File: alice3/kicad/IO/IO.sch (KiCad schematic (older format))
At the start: 1 part, among them U1 MiniM4-D40

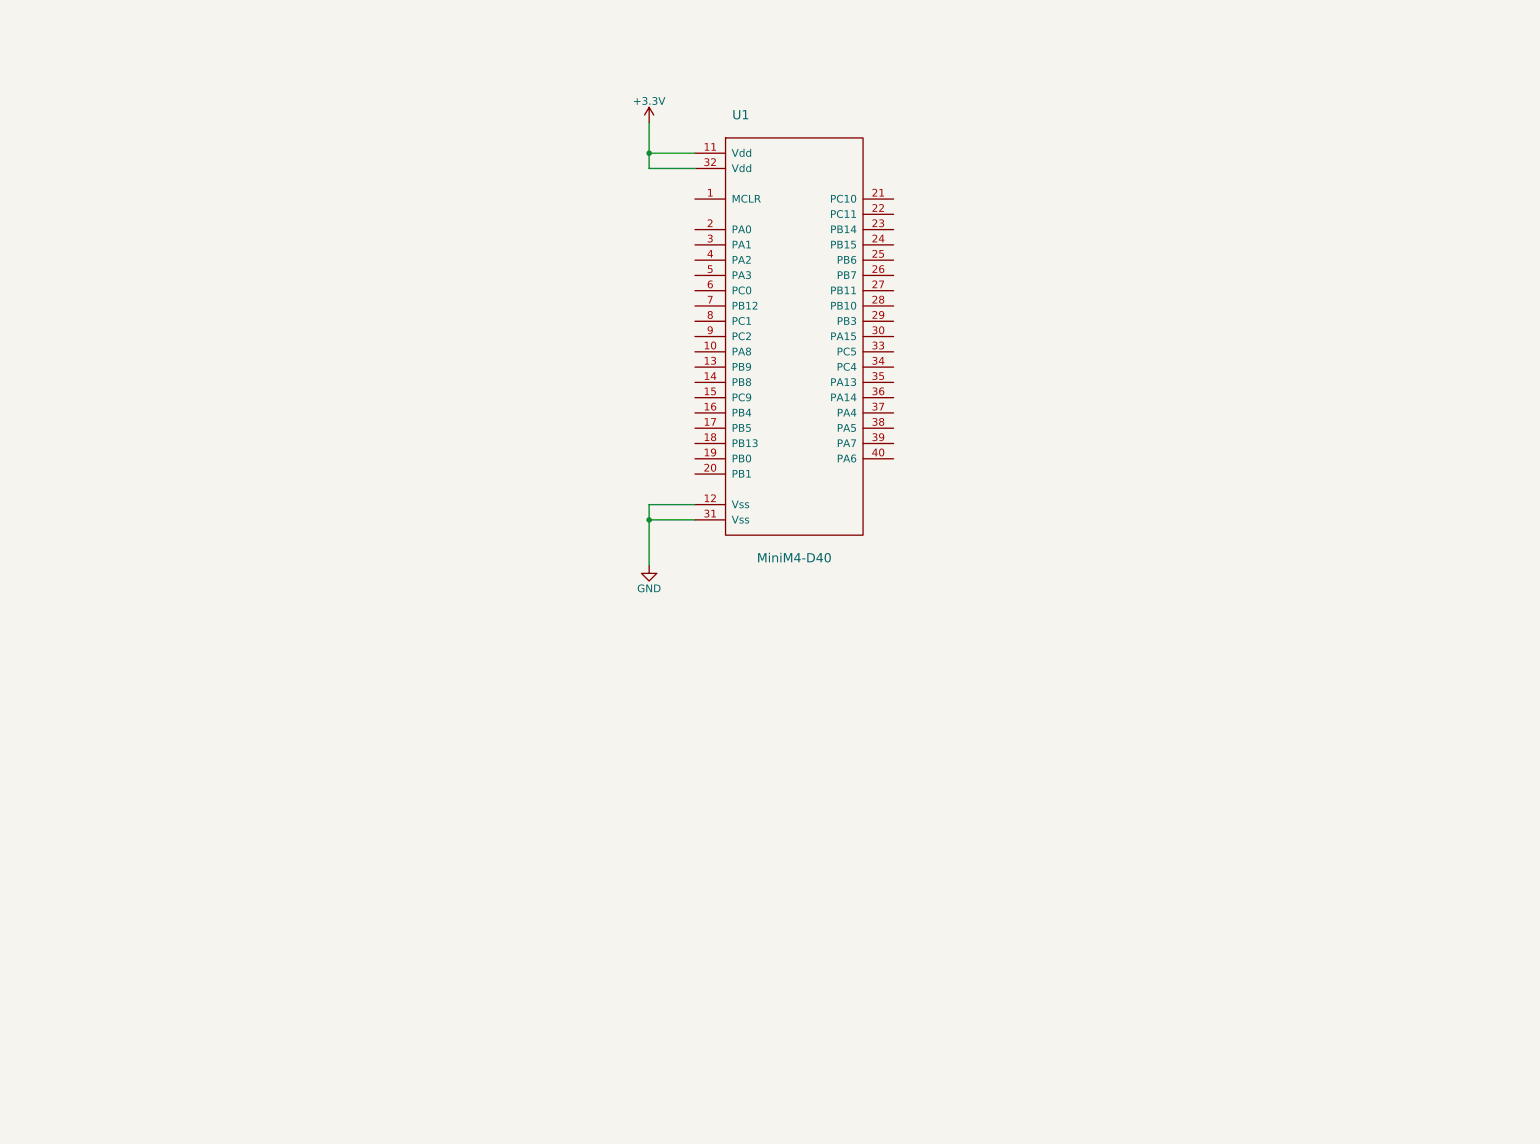
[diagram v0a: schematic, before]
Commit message: add SD socket to sch; level converter component
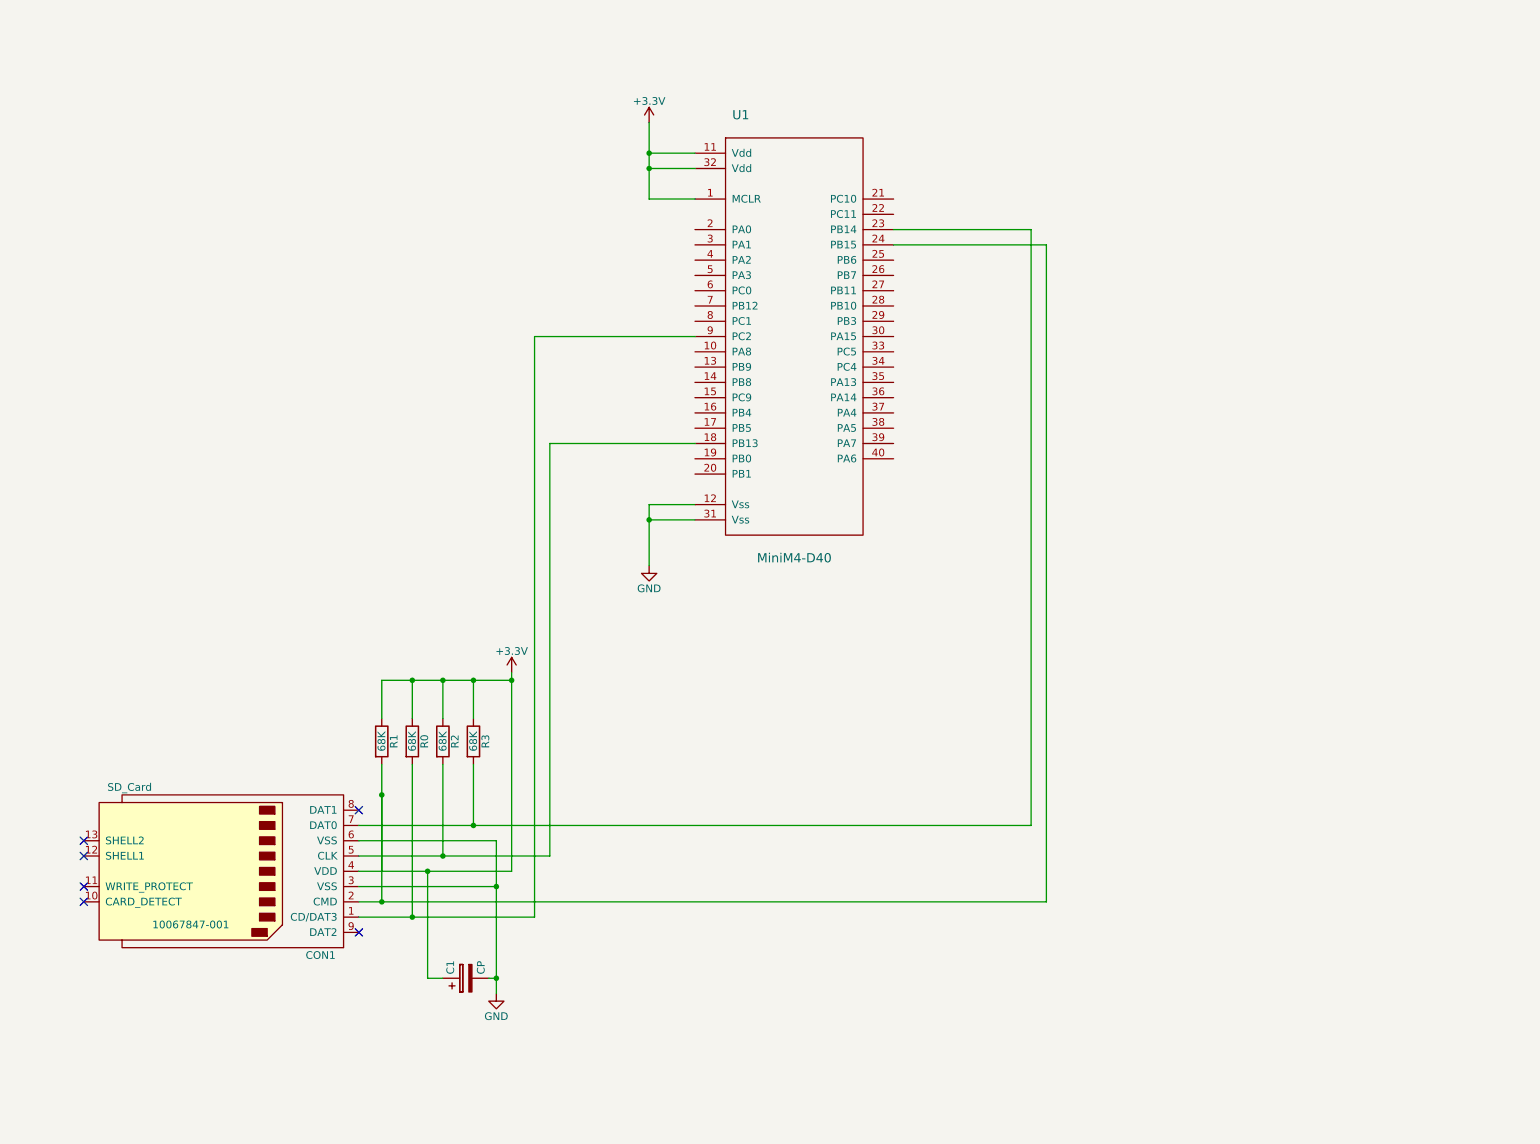
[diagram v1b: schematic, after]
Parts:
- added C1: CP, symbol CP
- added CON1: SD_Card, 10067847-001, symbol SD_Card
- added R0, R1, R2, R3: 68K, symbol R
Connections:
- net +3V3: now also U1.1 (MCLR), C1.1, CON1.4 (VDD), R0.1, R1.1, R2.1, R3.1
- net GND: now also C1.2, CON1.3 (VSS), CON1.6 (VSS)
- net at U1.18 (PB13): now also CON1.5 (CLK), R2.2
- net at U1.23 (PB14): now also CON1.7 (DAT0), R3.2
- net at U1.24 (PB15): now also CON1.2 (CMD), R1.2
- net at U1.9 (PC2): now also CON1.1 (CD/DAT3), R0.2
- no-connect marks 0 -> 6
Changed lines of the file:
@@
 LIBS:valves
 LIBS:minim4-d40
+LIBS:levelconverter
 LIBS:IO-cache
 EELAYER 25 0
@@
 $EndComp
 $Comp
-L +3.3V #PWR01
+L +3.3V #PWR3
 U 1 1 5689970E
 P 4800 1300
-F 0 "#PWR01" H 4800 1150 50  0001 C CNN
+F 0 "#PWR3" H 4800 1150 50  0001 C CNN
 F 1 "+3.3V" H 4800 1440 50  0000 C CNN
 F 2 "" H 4800 1300 60  0000 C CNN
@@
 	1    0    0    -1
 $EndComp
-Wire Wire Line
-	5100 1500 4800 1500
-Wire Wire Line
-	4800 1300 4800 1600
-Wire Wire Line
-	4800 1600 5100 1600
-Connection ~ 4800 1500
-$Comp
-L GND #PWR02
+$Comp
+L GND #PWR4
 U 1 1 5689975D
 P 4800 4200
-F 0 "#PWR02" H 4800 3950 50  0001 C CNN
+F 0 "#PWR4" H 4800 3950 50  0001 C CNN
 F 1 "GND" H 4800 4050 50  0000 C CNN
 F 2 "" H 4800 4200 60  0000 C CNN
@@
 	1    0    0    -1
 $EndComp
+$Comp
+L SD_Card CON1
+U 1 1 56899BB6
+P 2000 6200
+F 0 "CON1" H 1350 6750 50  0000 C CNN
+F 1 "SD_Card" H 2600 5650 50  0000 C CNN
+F 2 "10067847-001" H 2200 6550 50  0000 C CNN
+F 3 "" H 2000 6200 60  0000 C CNN
+	1    2000 6200
+	-1   0    0    1
+$EndComp
+NoConn ~ 1100 6000
+NoConn ~ 1100 6100
+NoConn ~ 1100 6300
+NoConn ~ 1100 6400
+NoConn ~ 2900 6600
+NoConn ~ 2900 5800
+$Comp
+L GND #PWR1
+U 1 1 56899C9B
+P 3800 7000
+F 0 "#PWR1" H 3800 6750 50  0001 C CNN
+F 1 "GND" H 3800 6850 50  0000 C CNN
+F 2 "" H 3800 7000 60  0000 C CNN
+F 3 "" H 3800 7000 60  0000 C CNN
+	1    3800 7000
+	1    0    0    -1
+$EndComp
+$Comp
+L +3.3V #PWR2
+U 1 1 56899CD4
+P 3900 4900
+F 0 "#PWR2" H 3900 4750 50  0001 C CNN
+F 1 "+3.3V" H 3900 5040 50  0000 C CNN
+F 2 "" H 3900 4900 60  0000 C CNN
+F 3 "" H 3900 4900 60  0000 C CNN
+	1    3900 4900
+	1    0    0    -1
+$EndComp
+Connection ~ 3800 6300
+Wire Wire Line
+	2900 6300 3800 6300
+Wire Wire Line
+	3800 6000 3800 7000
+Wire Wire Line
+	2900 6000 3800 6000
+Connection ~ 4800 1600
+Wire Wire Line
+	4800 1800 5100 1800
+Connection ~ 4800 3900
+Wire Wire Line
+	5100 3900 4800 3900
+Wire Wire Line
+	4800 3800 4800 4200
 Wire Wire Line
 	5100 3800 4800 3800
-Wire Wire Line
-	4800 3800 4800 4200
-Wire Wire Line
-	5100 3900 4800 3900
-Connection ~ 4800 3900
+Connection ~ 4800 1500
+Wire Wire Line
+	4800 1600 5100 1600
+Wire Wire Line
+	4800 1300 4800 1800
+Wire Wire Line
+	5100 1500 4800 1500
+Wire Wire Line
+	5100 2700 4050 2700
+Wire Wire Line
+	4050 2700 4050 6500
+Wire Wire Line
+	4050 6500 2900 6500
+Wire Wire Line
+	2900 6400 7400 6400
+Wire Wire Line
+	7400 6400 7400 2100
+Wire Wire Line
+	7400 2100 6400 2100
+Wire Wire Line
+	5100 3400 4150 3400
+Wire Wire Line
+	4150 3400 4150 6100
+Wire Wire Line
+	4150 6100 2900 6100
+Wire Wire Line
+	2900 5900 7300 5900
+Wire Wire Line
+	7300 5900 7300 2000
+Wire Wire Line
+	7300 2000 6400 2000
+$Comp
+L R R0
+U 1 1 5689A6F4
+P 3250 5350
+F 0 "R0" V 3330 5350 50  0000 C CNN
+F 1 "68K" V 3250 5350 50  0000 C CNN
+F 2 "" V 3180 5350 30  0000 C CNN
+F 3 "" H 3250 5350 30  0000 C CNN
+	1    3250 5350
+	1    0    0    -1
+$EndComp
+Connection ~ 3050 6400
+$Comp
+L R R1
+U 1 1 5689A7DE
+P 3050 5350
+F 0 "R1" V 3130 5350 50  0000 C CNN
+F 1 "68K" V 3050 5350 50  0000 C CNN
+F 2 "" V 2980 5350 30  0000 C CNN
+F 3 "" H 3050 5350 30  0000 C CNN
+	1    3050 5350
+	1    0    0    -1
+$EndComp
+$Comp
+L R R2
+U 1 1 5689A7FF
+P 3450 5350
+F 0 "R2" V 3530 5350 50  0000 C CNN
+F 1 "68K" V 3450 5350 50  0000 C CNN
+F 2 "" V 3380 5350 30  0000 C CNN
+F 3 "" H 3450 5350 30  0000 C CNN
+	1    3450 5350
+	1    0    0    -1
+$EndComp
+Wire Wire Line
+	3900 6200 3900 4900
+$Comp
+L R R3
+U 1 1 5689A887
+P 3650 5350
+F 0 "R3" V 3730 5350 50  0000 C CNN
+F 1 "68K" V 3650 5350 50  0000 C CNN
+F 2 "" V 3580 5350 30  0000 C CNN
+F 3 "" H 3650 5350 30  0000 C CNN
+	1    3650 5350
+	1    0    0    -1
+$EndComp
+Wire Wire Line
+	3050 5500 3050 6400
+Wire Wire Line
+	3450 5500 3450 6100
+Connection ~ 3450 6100
+Wire Wire Line
+	3650 5500 3650 5900
+Connection ~ 3650 5900
+Wire Wire Line
+	3050 5200 3050 4950
+Wire Wire Line
+	3050 4950 3900 4950
+Connection ~ 3900 4950
+Wire Wire Line
+	3250 5200 3250 4950
+Connection ~ 3250 4950
+Wire Wire Line
+	3450 4950 3450 5200
+Connection ~ 3450 4950
+Wire Wire Line
+	3650 5200 3650 4950
+Connection ~ 3650 4950
+Wire Wire Line
+	3050 5700 3050 6200
+Connection ~ 3050 5700
+Wire Wire Line
+	2900 6200 3900 6200
+Wire Wire Line
+	3250 5500 3250 6500
+Connection ~ 3250 6500
+$Comp
+L CP C1
+U 1 1 5689AB18
+P 3600 6900
+F 0 "C1" H 3625 7000 50  0000 L CNN
+F 1 "CP" H 3625 6800 50  0000 L CNN
+F 2 "" H 3638 6750 30  0000 C CNN
+F 3 "" H 3600 6900 60  0000 C CNN
+	1    3600 6900
+	0    -1   -1   0
+$EndComp
+Wire Wire Line
+	3450 6900 3350 6900
+Wire Wire Line
+	3350 6900 3350 6200
+Connection ~ 3350 6200
+Wire Wire Line
+	3750 6900 3800 6900
+Connection ~ 3800 6900
 $EndSCHEMATC

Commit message: connect Alice 3 bus through level converters to MiniM4
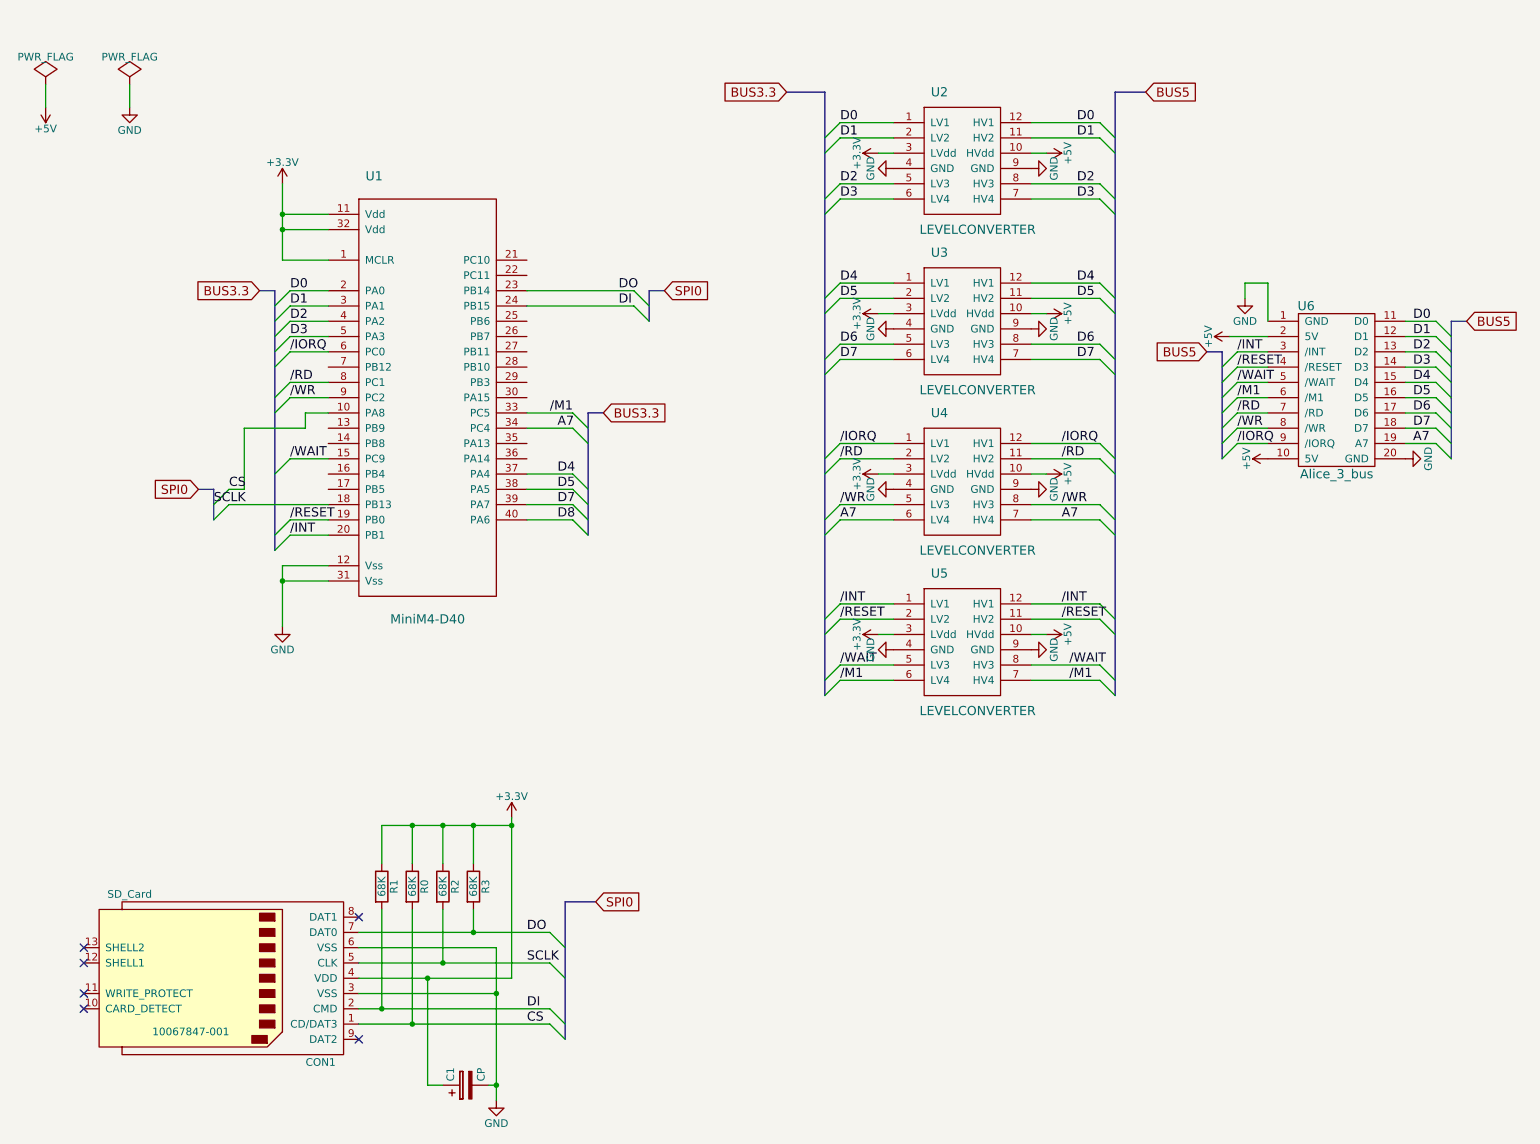
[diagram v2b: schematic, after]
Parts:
- added U2, U3, U4, U5: LEVELCONVERTER, symbol LEVELCONVERTER
- added U6: Alice_3_bus, symbol Alice_3_bus
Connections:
- net +3V3: now also U2.3 (LVdd), U3.3 (LVdd), U4.3 (LVdd), U5.3 (LVdd)
- net GND: now also U2.4 (GND), U2.9 (GND), U3.4 (GND), U3.9 (GND), U4.4 (GND), U4.9 (GND), U5.4 (GND), U5.9 (GND), U6.1 (GND), U6.20 (GND)
- net CS: now reaches U1.10 (PA8)
- net CS: now also CON1.1 (CD/DAT3), R0.2
- net /WAIT: now reaches U1.15 (PC9)
- net /WAIT: now also U5.5 (LV3), U5.8 (HV3), U6.5 (/WAIT)
- net SCLK: now reaches CON1.5 (CLK), R2.2
- net SCLK: no longer U1.18 (PB13)
- net /RESET: now reaches U1.19 (PB0)
- net /RESET: now also U5.11 (HV2), U5.2 (LV2), U6.4 (/RESET)
- net D0: now reaches U1.2 (PA0)
- net D0: now also U2.1 (LV1), U2.12 (HV1), U6.11 (D0)
- net /INT: now reaches U1.20 (PB1)
- net /INT: now also U5.1 (LV1), U5.12 (HV1), U6.3 (/INT)
- net DO: now reaches CON1.7 (DAT0), R3.2, U1.23 (PB14)
- net DI: now reaches CON1.2 (CMD), R1.2, U1.24 (PB15)
- net D1: now reaches U1.3 (PA1)
- net D1: now also U2.11 (HV2), U2.2 (LV2), U6.12 (D1)
- net /M1: now reaches U1.33 (PC5)
- net /M1: now also U5.6 (LV4), U5.7 (HV4), U6.6 (/M1)
- net A7: now reaches U1.34 (PC4)
- net A7: now also U4.6 (LV4), U4.7 (HV4), U6.19 (A7)
- net D4: now reaches U1.37 (PA4)
- net D4: now also U3.1 (LV1), U3.12 (HV1), U6.15 (D4)
- net D5: now reaches U1.38 (PA5)
- net D5: now also U3.11 (HV2), U3.2 (LV2), U6.16 (D5)
- net D7: now reaches U1.39 (PA7)
- net D7: now also U3.6 (LV4), U3.7 (HV4), U6.18 (D7)
- net D2: now reaches U1.4 (PA2)
- net D2: now also U2.5 (LV3), U2.8 (HV3), U6.13 (D2)
- net D8: now reaches U1.40 (PA6)
- net D3: now reaches U1.5 (PA3)
- net D3: now also U2.6 (LV4), U2.7 (HV4), U6.14 (D3)
- net /IORQ: now reaches U1.6 (PC0)
- net /IORQ: now also U4.1 (LV1), U4.12 (HV1), U6.9 (/IORQ)
- net /RD: now reaches U1.8 (PC1)
- net /RD: now also U4.11 (HV2), U4.2 (LV2), U6.7 (/RD)
- new net +5V: U2.10 (HVdd), U3.10 (HVdd), U4.10 (HVdd), U5.10 (HVdd), U6.10 (5V), U6.2 (5V)
- new net /WR: U1.9 (PC2), U4.5 (LV3), U4.8 (HV3), U6.8 (/WR)
- new net D6: U3.5 (LV3), U3.8 (HV3), U6.17 (D6)
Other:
- moved on the sheet: C1, CON1, R0, R1, R2, R3, U1

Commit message: first draft of complete IO board schematic
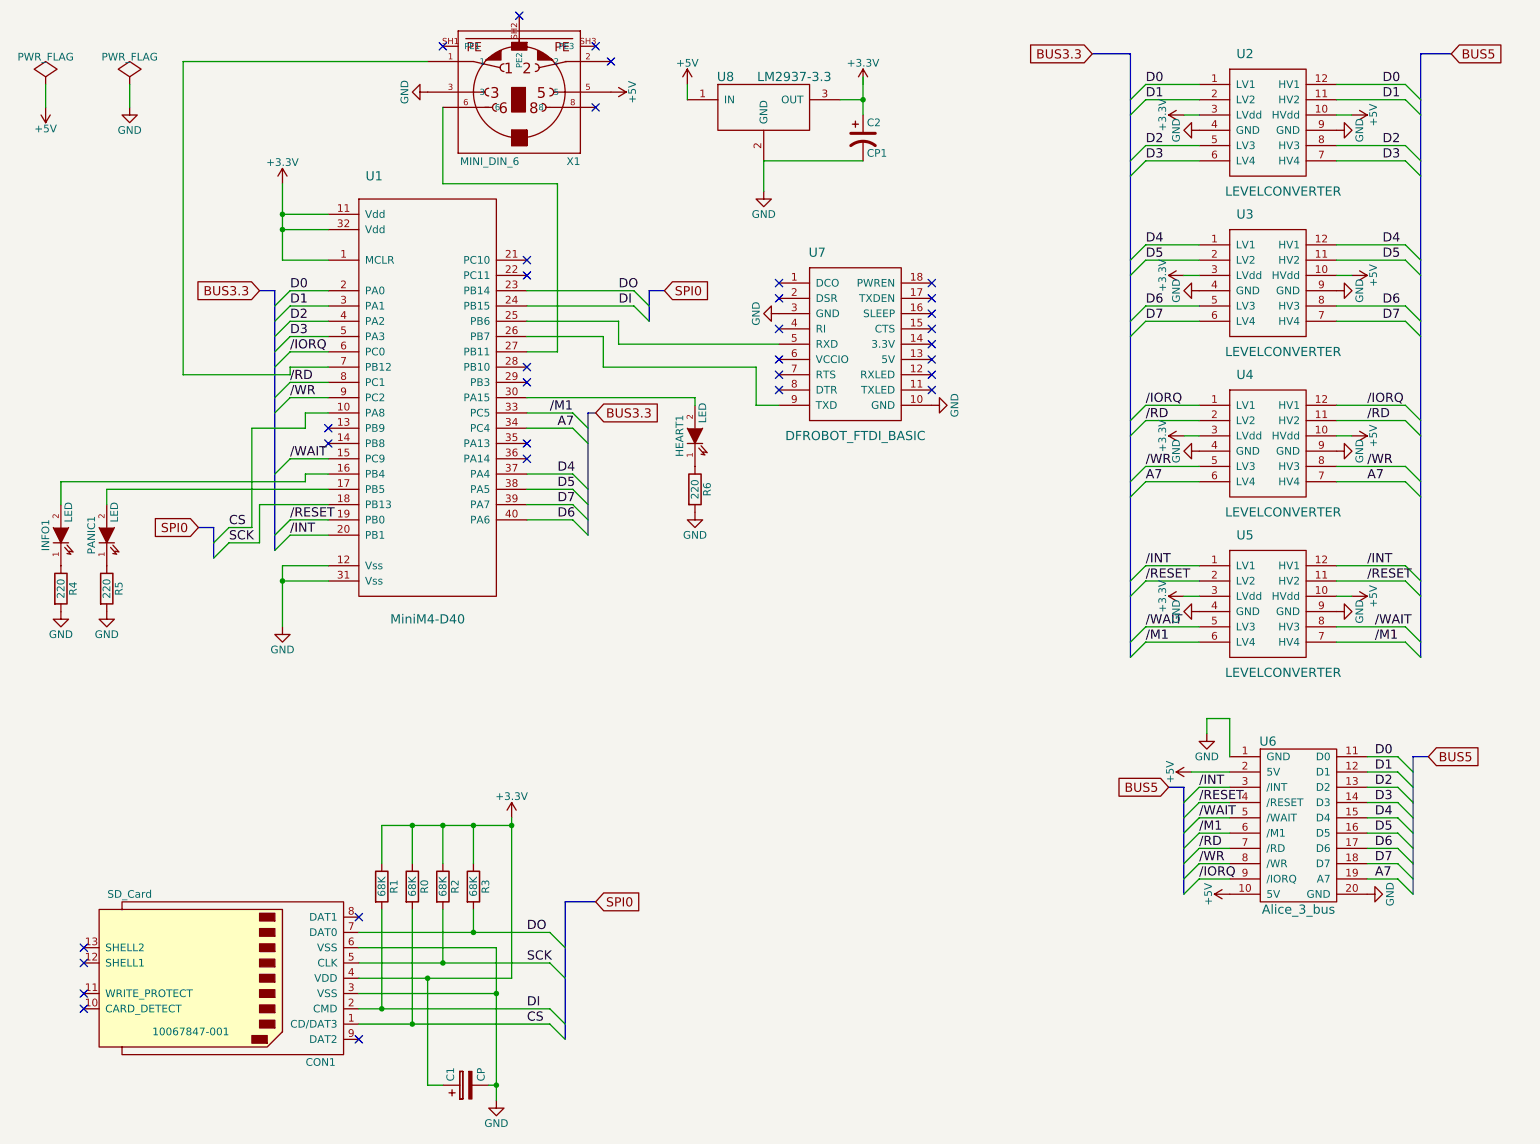
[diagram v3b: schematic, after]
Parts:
- added C2: CP1, symbol CP1
- added HEART1, INFO1, PANIC1: LED, symbol LED
- added R4, R5, R6: 220, symbol R
- added U7: DFROBOT_FTDI_BASIC, symbol DFROBOT_FTDI_BASIC
- added U8: LM2937-3.3, symbol LM2937-3.3
- added X1: MINI_DIN_6, mini_din-M_DIN6, symbol MINI_DIN_6
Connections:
- net D8 is gone; now on net D6: U1.40 (PA6)
- net SCLK is gone; now on net SCK: CON1.5 (CLK), R2.2
- net +5V: now also U8.1 (IN), X1.5
- net GND: now also C2.2, R4.2, R5.2, R6.2, U7.10 (GND), U7.3 (GND), U8.2 (GND), X1.3
- net at U1.16 (PB4): now also INFO1.2 (A)
- net at U1.17 (PB5): now also PANIC1.2 (A)
- net SCK: now reaches U1.18 (PB13)
- net at U1.25 (PB6): now also U7.5 (RXD)
- net at U1.26 (PB7): now also U7.9 (TXD)
- net at U1.27 (PB11): now also X1.6
- net at U1.30 (PA15): now also HEART1.2 (A)
- net at U1.7 (PB12): now also X1.1
- new net: HEART1.1 (K), R6.1
- new net: PANIC1.1 (K), R5.1
- new net: INFO1.1 (K), R4.1
- new net: C2.1, U8.3 (OUT)
- no-connect marks 6 -> 33
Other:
- moved on the sheet: U2, U3, U4, U5, U6
